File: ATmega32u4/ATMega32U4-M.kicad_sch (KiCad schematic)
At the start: 19 parts, among them U2 ATmega32U4-M, Y1 16MHz

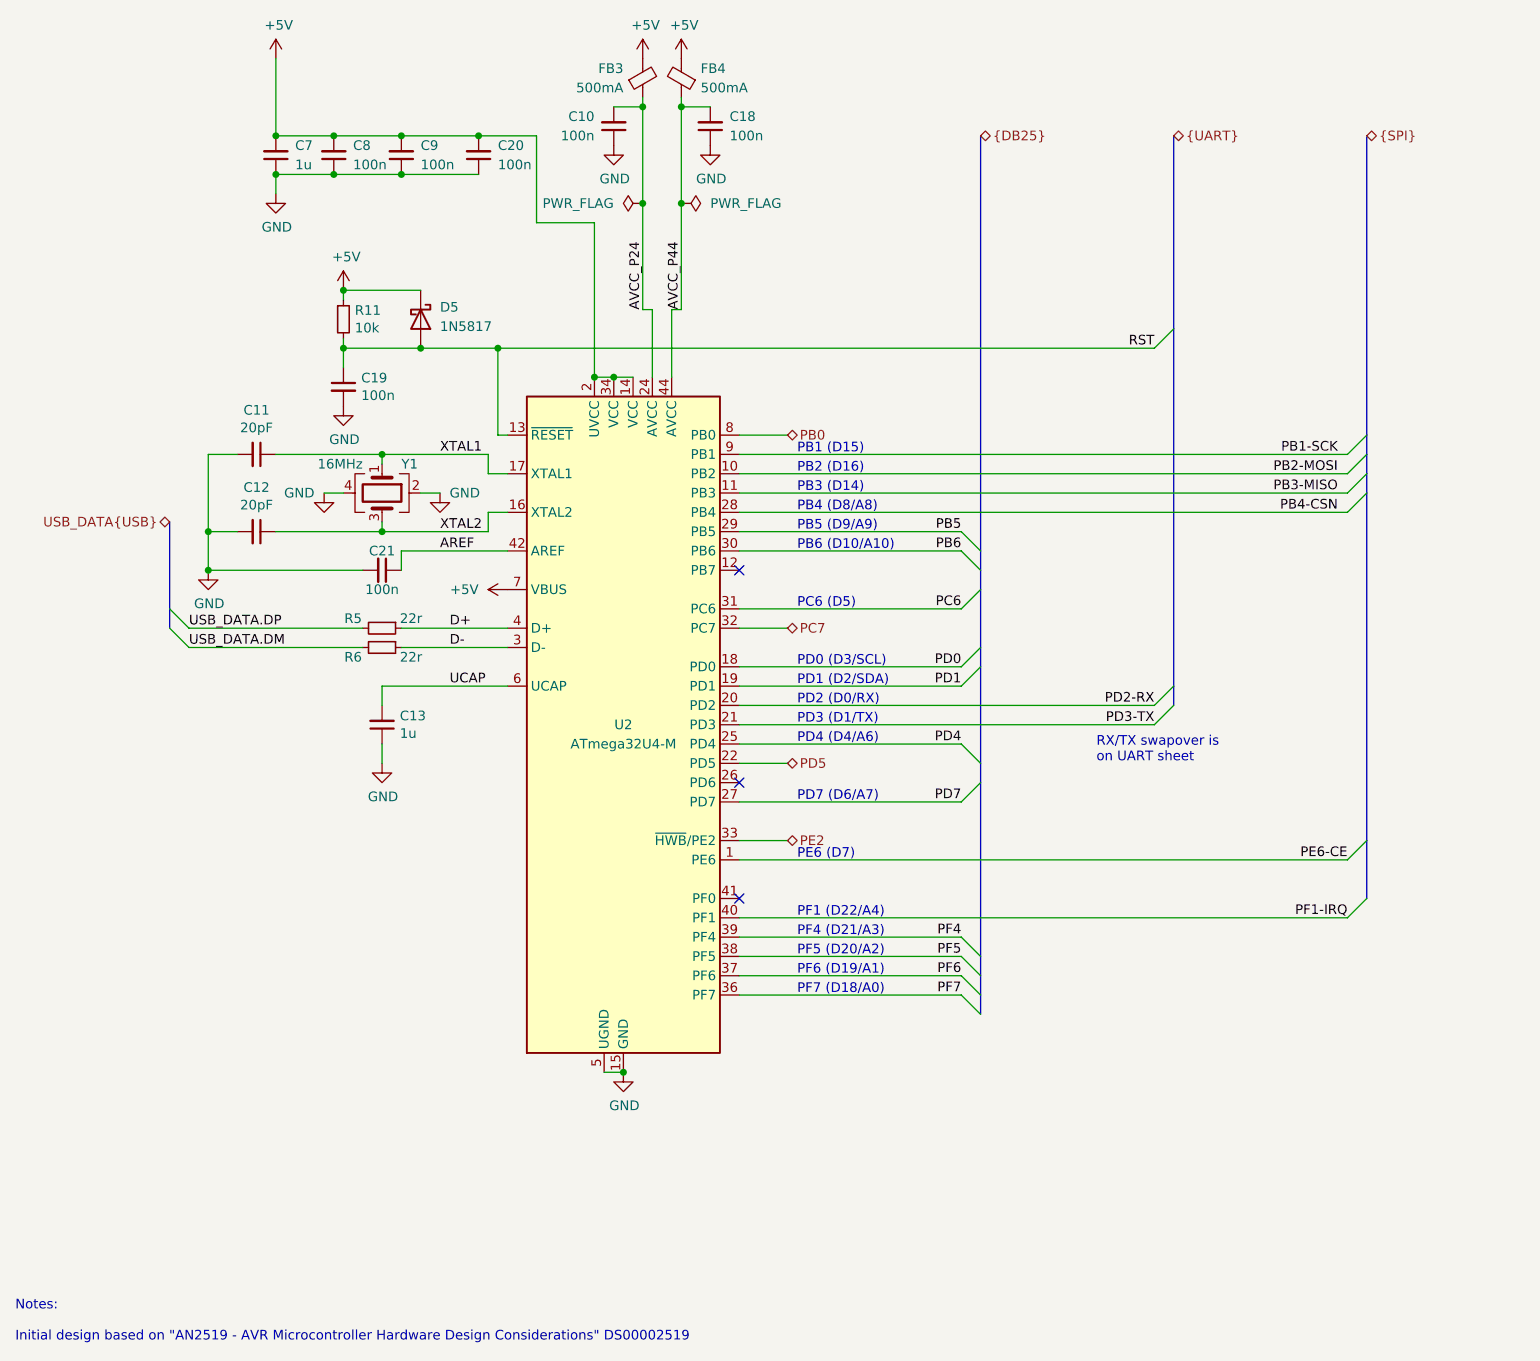
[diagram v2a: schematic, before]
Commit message: Update notes, add io for reading cc pins, minor changes to schematic and routing.
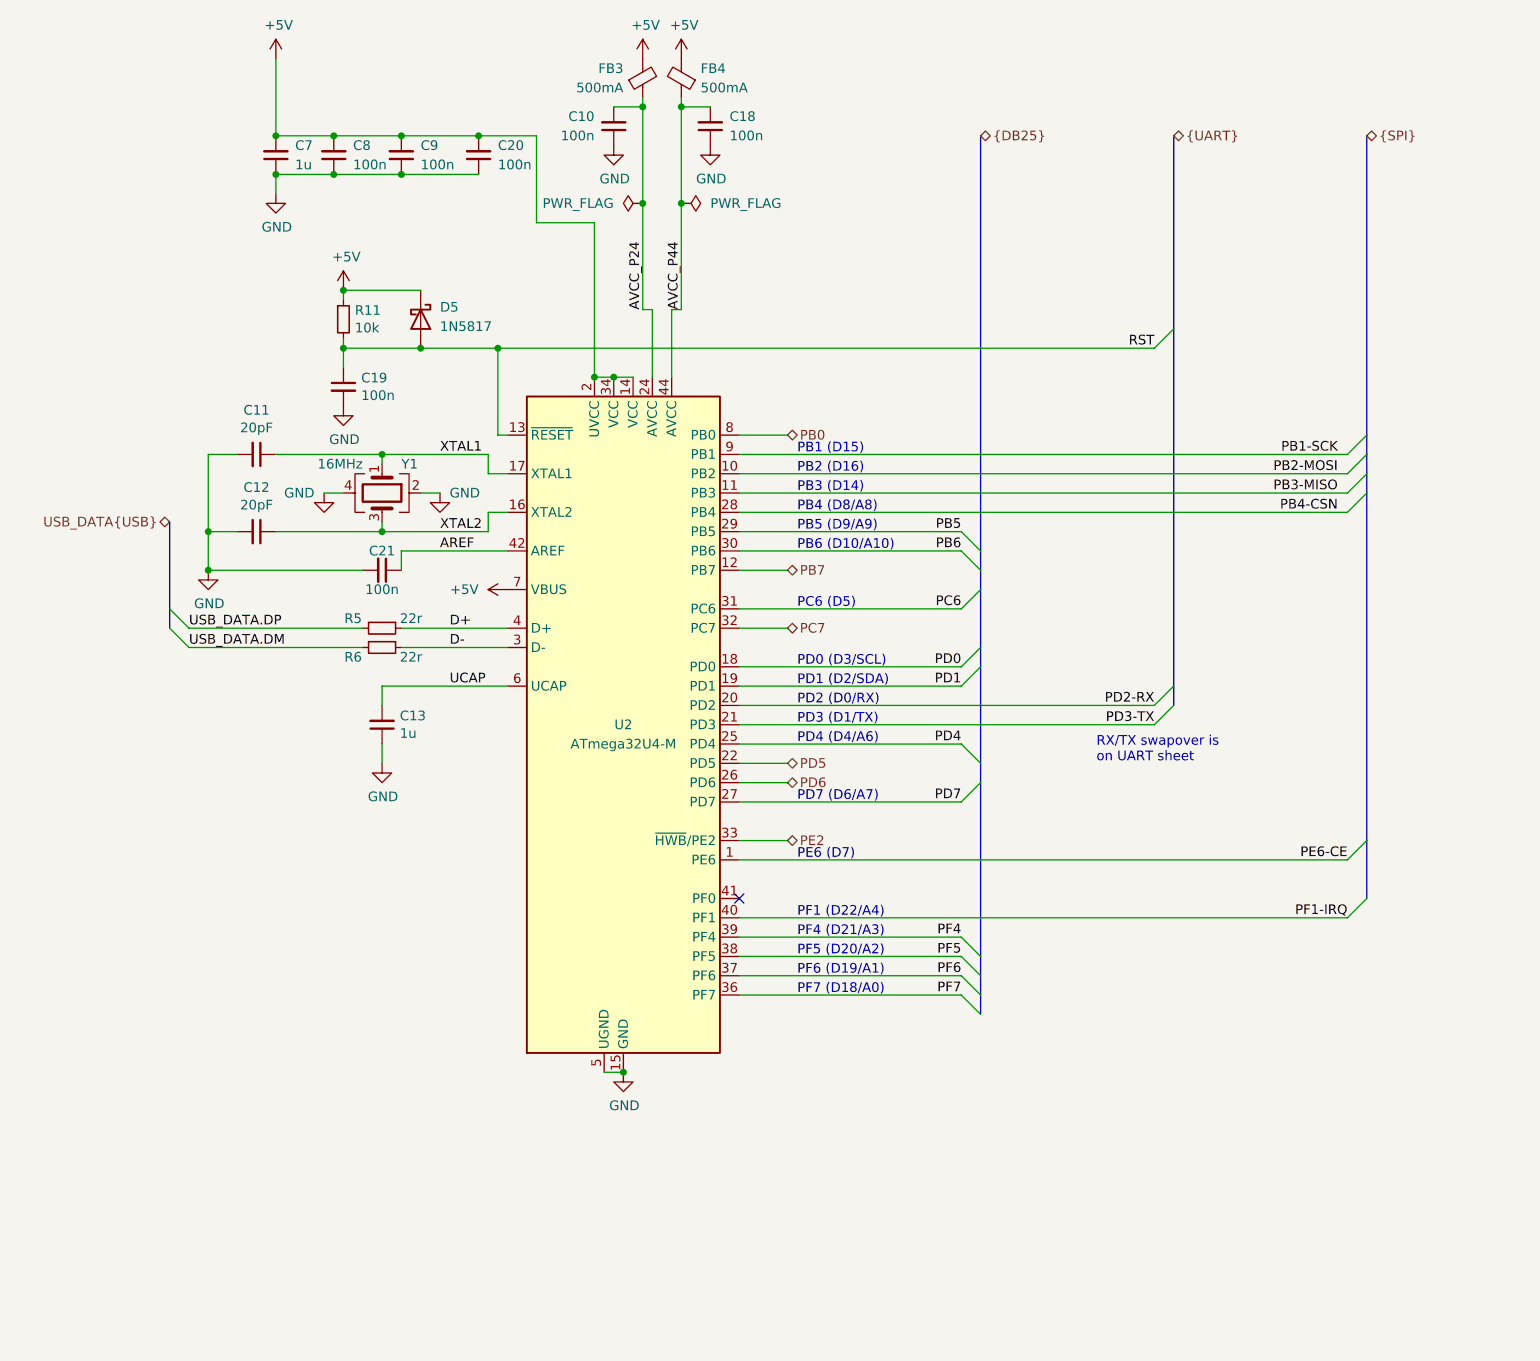
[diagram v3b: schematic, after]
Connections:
- net PB7: now reaches U2.12 (PB7)
- net PD6: now reaches U2.26 (PD6)
- no-connect marks 3 -> 1
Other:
- note removed: "Notes: Initial design based on "AN2519 - AVR Microcontroller Hardware Design Considerations" DS00002519"
- title: (none) -> OpenRetroPad
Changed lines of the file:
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@@
 (kicad_sch (version 20211123) (generator eeschema)
   (paper "A4")
+  (title_block
+    (title "OpenRetroPad")
+    (date "2022-12-29")
+    (rev "2")
+    (comment 3 "github.com/OpenRetroPad")
+    (comment 4 "ATmega32u4")
+  )
   (junction (at 63.5 43.18) (diameter 0) (color 0 0 0 0)
   )
@@
   (junction (at 91.44 69.85) (diameter 0) (color 0 0 0 0)
   )
-  (no_connect (at 107.95 95.25))
-  (no_connect (at 107.95 123.19))
   (no_connect (at 107.95 138.43))
   (bus_entry (at 187.96 80.01) (size 2.54 -2.54)
@@
     (stroke (width 0) (type default) (color 0 0 0 0))
   )
+  (wire (pts (xy 107.95 95.25) (xy 114.3 95.25))
+    (stroke (width 0) (type default) (color 0 0 0 0))
+  )
   (wire (pts (xy 100.33 46.99) (xy 100.33 60.96))
     (stroke (width 0) (type default) (color 0 0 0 0))
@@
     (stroke (width 0) (type default) (color 0 0 0 0))
   )
+  (wire (pts (xy 107.95 123.19) (xy 114.3 123.19))
+    (stroke (width 0) (type default) (color 0 0 0 0))
+  )
   (wire (pts (xy 60.96 120.65) (xy 60.96 118.11))
     (stroke (width 0) (type default) (color 0 0 0 0))
@@
   )
   (text "PD7 (D6/A7)" (at 115.57 125.73 0)
-    (effects (font (size 1.27 1.27)) (justify left bottom))
-  )
-  (text "Notes:\n\nInitial design based on \"AN2519 - AVR Microcontroller Hardware Design Considerations\" DS00002519 "
-    (at 12.7 196.85 0)
     (effects (font (size 1.27 1.27)) (justify left bottom))
   )
@@
     (effects (font (size 1.27 1.27)) (justify right))
   )
+  (hierarchical_label "PB7" (shape bidirectional) (at 114.3 95.25 0)
+    (effects (font (size 1.27 1.27)) (justify left))
+  )
+  (hierarchical_label "PD6" (shape bidirectional) (at 114.3 123.19 0)
+    (effects (font (size 1.27 1.27)) (justify left))
+  )
   (hierarchical_label "{UART}" (shape bidirectional) (at 165.1 38.1 0)

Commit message: Change CC pin <-> ADC pin, adjust routing
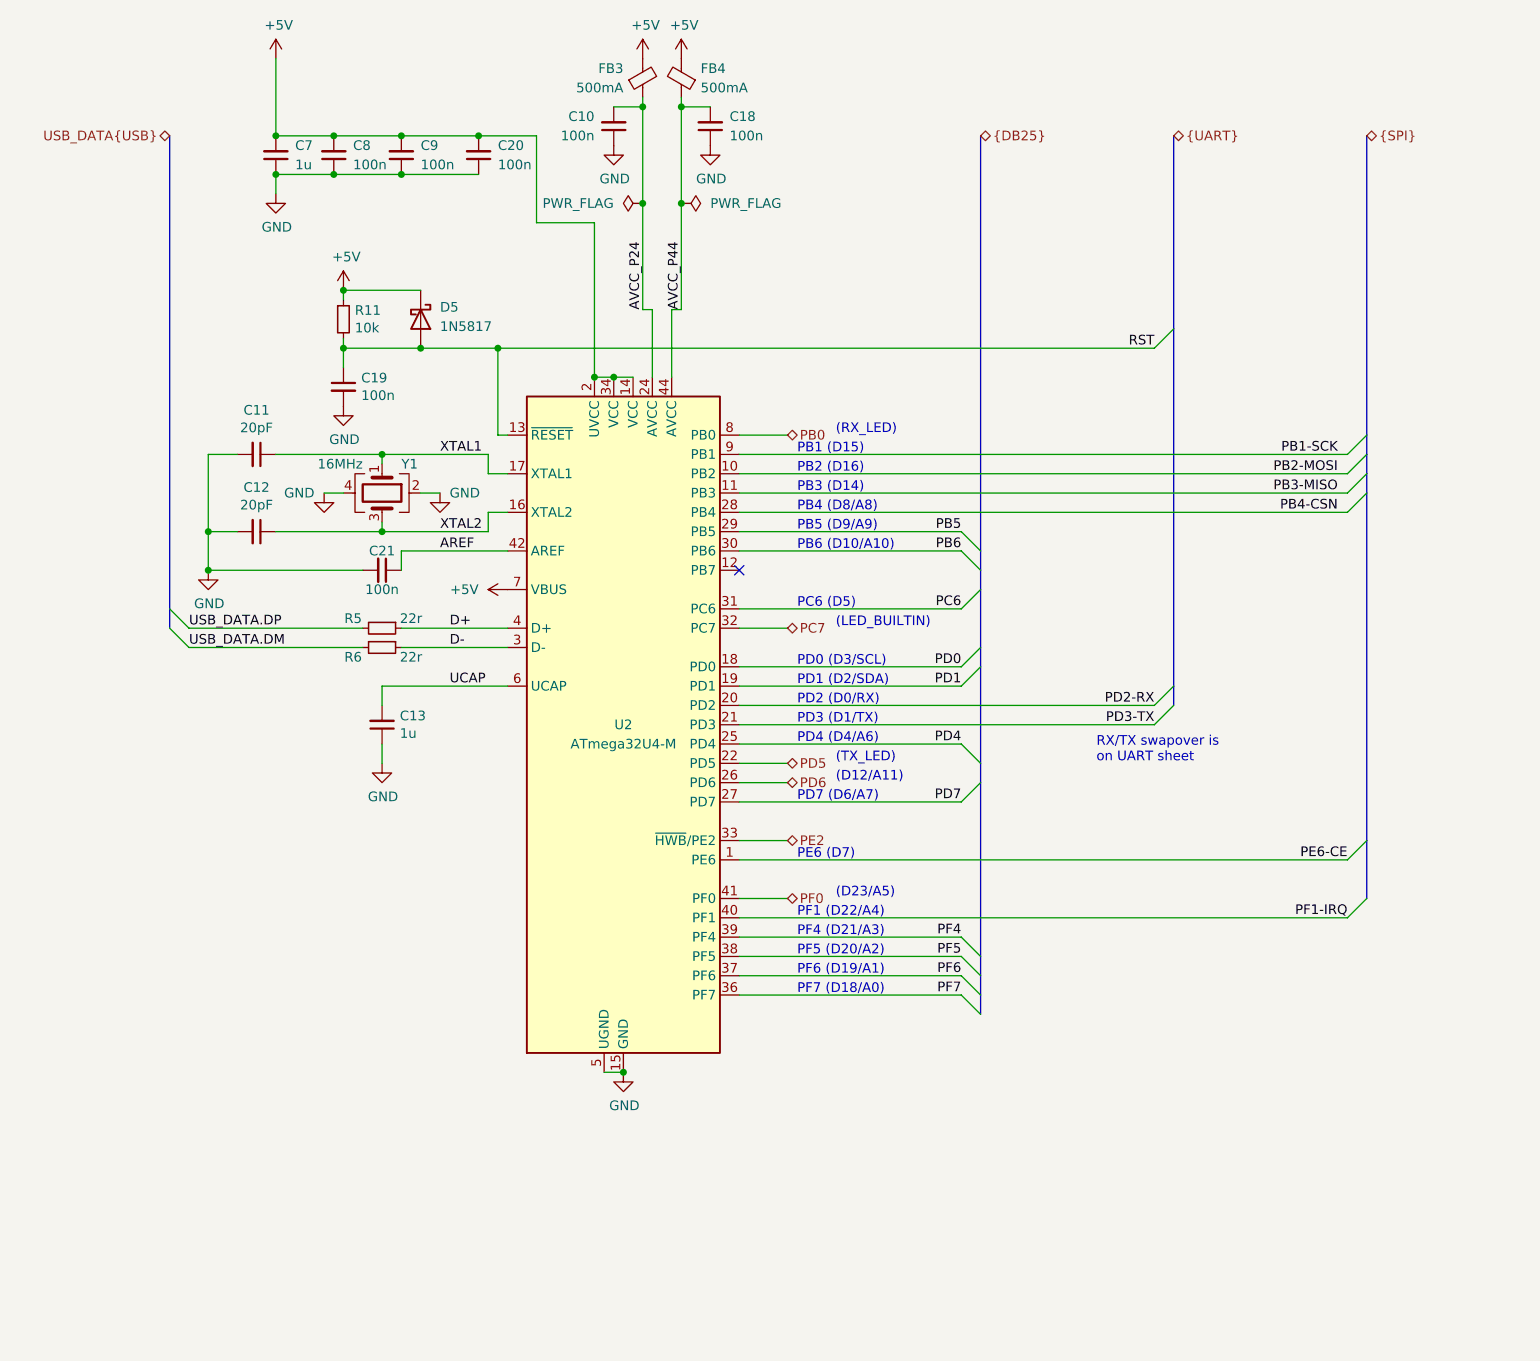
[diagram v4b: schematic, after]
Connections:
- net PF0: now reaches U2.41 (PF0)
- net PB7: no longer names the net of U2.12 (PB7)
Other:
- note added: "(D12/A11)"
- note added: "(D23/A5)"
- note added: "(LED_BUILTIN)"
- note added: "(RX_LED)"
- note added: "(TX_LED)"
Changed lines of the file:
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@@
   (junction (at 91.44 69.85) (diameter 0) (color 0 0 0 0)
   )
-  (no_connect (at 107.95 138.43))
+  (no_connect (at 107.95 95.25))
   (bus_entry (at 187.96 80.01) (size 2.54 -2.54)
     (stroke (width 0) (type default) (color 0 0 0 0))
@@
     (stroke (width 0) (type default) (color 0 0 0 0))
   )
-  (wire (pts (xy 107.95 95.25) (xy 114.3 95.25))
-    (stroke (width 0) (type default) (color 0 0 0 0))
-  )
   (wire (pts (xy 100.33 46.99) (xy 100.33 60.96))
     (stroke (width 0) (type default) (color 0 0 0 0))
@@
     (stroke (width 0) (type default) (color 0 0 0 0))
   )
-  (bus (pts (xy 33.02 88.9) (xy 33.02 100.33))
+  (bus (pts (xy 33.02 38.1) (xy 33.02 100.33))
     (stroke (width 0) (type default) (color 0 0 0 0))
   )
@@
     (stroke (width 0) (type default) (color 0 0 0 0))
   )
+  (wire (pts (xy 107.95 138.43) (xy 114.3 138.43))
+    (stroke (width 0) (type default) (color 0 0 0 0))
+  )
   (wire (pts (xy 77.47 77.47) (xy 76.2 77.47))
     (stroke (width 0) (type default) (color 0 0 0 0))
@@
     (effects (font (size 1.27 1.27)) (justify left bottom))
   )
+  (text "(D23/A5)" (at 120.65 138.43 0)
+    (effects (font (size 1.27 1.27)) (justify left bottom))
+  )
   (text "PB6 (D10/A10)" (at 115.57 92.71 0)
     (effects (font (size 1.27 1.27)) (justify left bottom))
@@
     (effects (font (size 1.27 1.27)) (justify left bottom))
   )
+  (text "(D12/A11)" (at 120.65 123.19 0)
+    (effects (font (size 1.27 1.27)) (justify left bottom))
+  )
   (text "PB1 (D15)" (at 115.57 80.01 0)
     (effects (font (size 1.27 1.27)) (justify left bottom))
@@
     (effects (font (size 1.27 1.27)) (justify left bottom))
   )
+  (text "(LED_BUILTIN)" (at 120.65 102.87 0)
+    (effects (font (size 1.27 1.27)) (justify left bottom))
+  )
   (text "PF1 (D22/A4)" (at 115.57 140.97 0)
     (effects (font (size 1.27 1.27)) (justify left bottom))
@@
     (effects (font (size 1.27 1.27)) (justify left bottom))
   )
+  (text "(RX_LED)" (at 120.65 77.47 0)
+    (effects (font (size 1.27 1.27)) (justify left bottom))
+  )
   (text "PF6 (D19/A1)" (at 115.57 148.59 0)
     (effects (font (size 1.27 1.27)) (justify left bottom))
@@
   )
   (text "PD2 (D0/RX)" (at 115.57 113.03 0)
+    (effects (font (size 1.27 1.27)) (justify left bottom))
+  )
+  (text "(TX_LED)" (at 120.65 120.65 0)
     (effects (font (size 1.27 1.27)) (justify left bottom))
   )
@@
     (effects (font (size 1.27 1.27)) (justify left))
   )
-  (hierarchical_label "USB_DATA{USB}" (shape bidirectional) (at 33.02 88.9 180)
+  (hierarchical_label "USB_DATA{USB}" (shape bidirectional) (at 33.02 38.1 180)
     (effects (font (size 1.27 1.27)) (justify right))
-  )
-  (hierarchical_label "PB7" (shape bidirectional) (at 114.3 95.25 0)
-    (effects (font (size 1.27 1.27)) (justify left))
   )
   (hierarchical_label "PD6" (shape bidirectional) (at 114.3 123.19 0)
@@
     (effects (font (size 1.27 1.27)) (justify left))
   )
+  (hierarchical_label "PF0" (shape bidirectional) (at 114.3 138.43 0)
+    (effects (font (size 1.27 1.27)) (justify left))
+  )
